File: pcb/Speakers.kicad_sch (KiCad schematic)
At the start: 34 parts, among them U4 ADA4891, U7 ADA4891

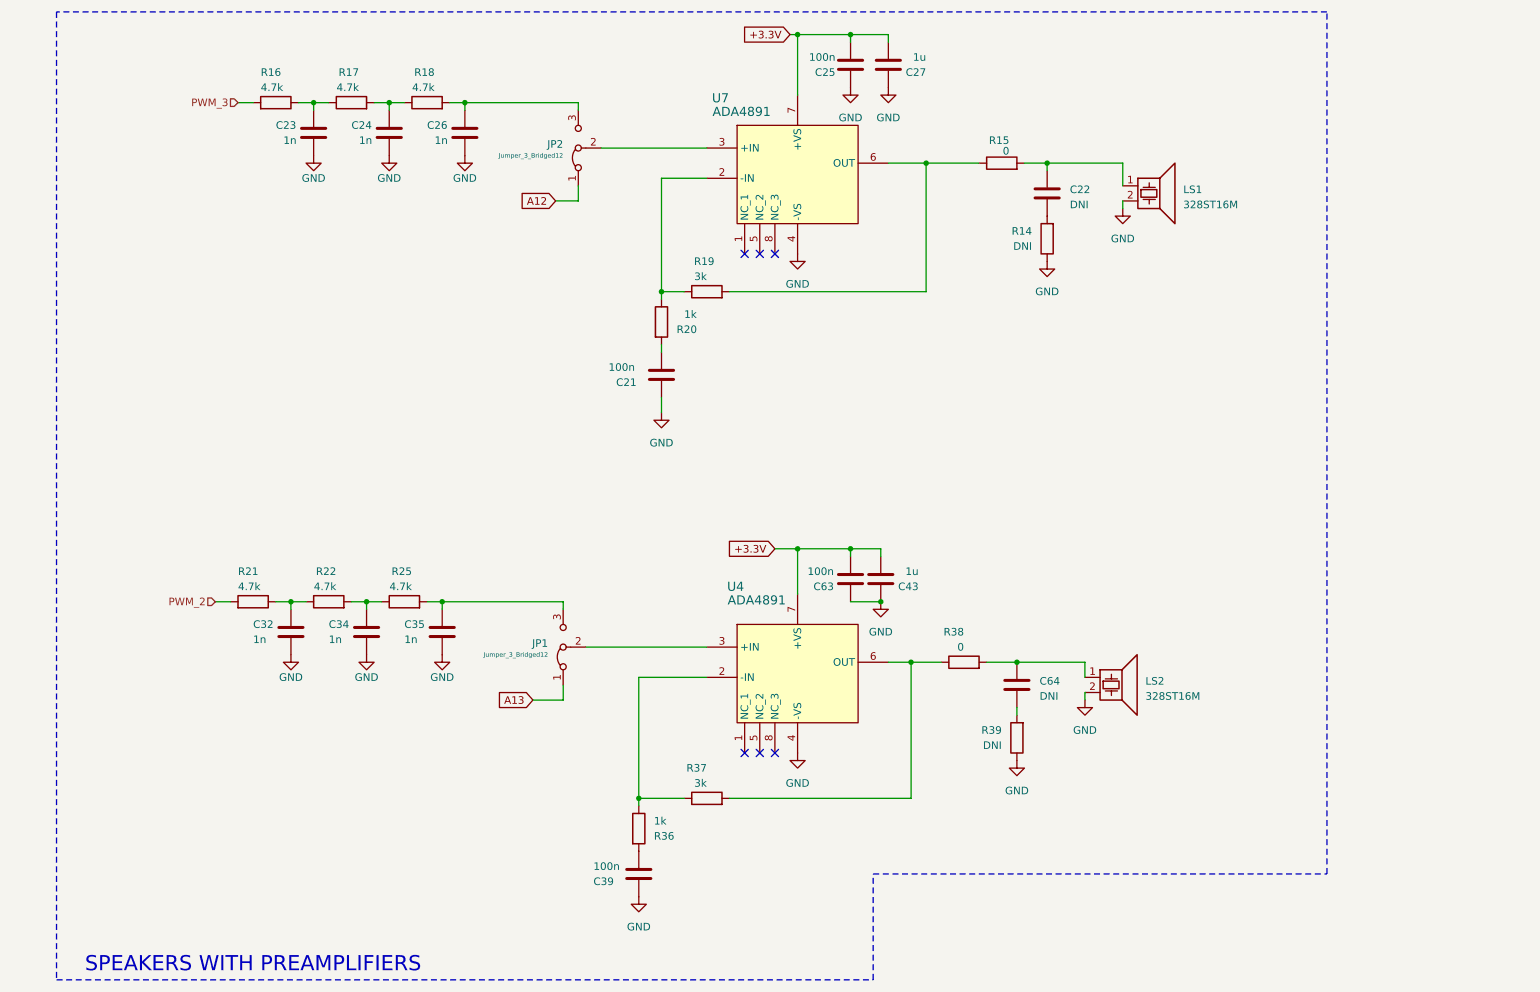
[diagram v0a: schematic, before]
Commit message: Progress in pcb routing
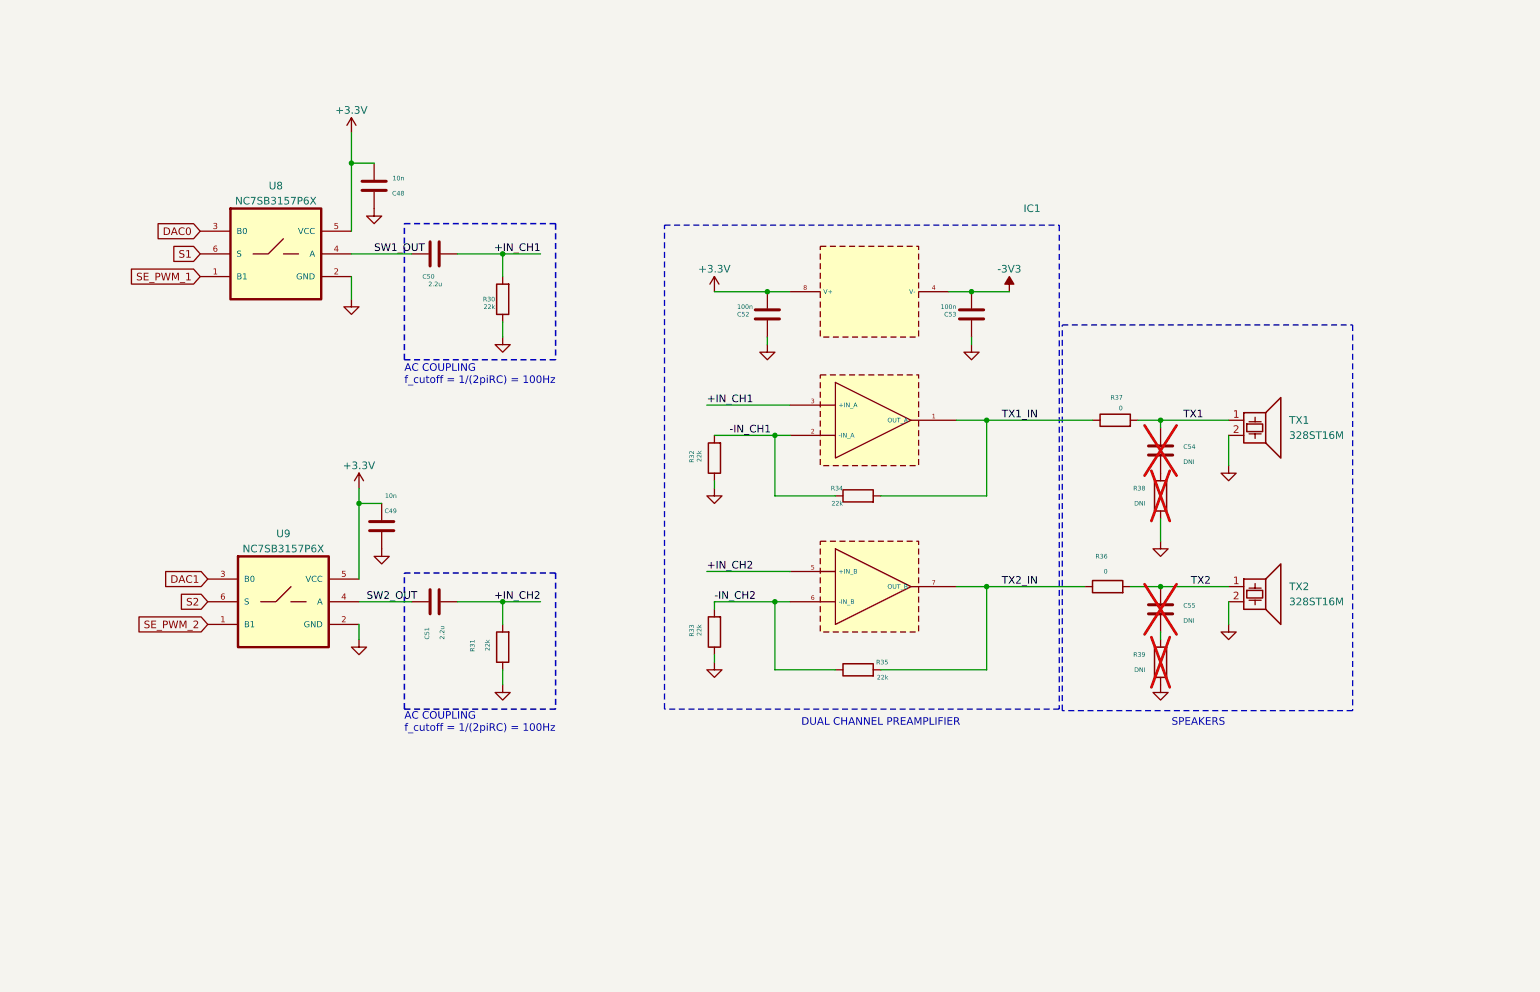
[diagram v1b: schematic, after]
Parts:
- removed C21, C25, C39, C63: 100n, Capacitor_SMD:C_0805_2012Metric, symbol Device:C
- removed C23, C24, C26, C32, C34, C35: 1n, Capacitor_SMD:C_0805_2012Metric, symbol Device:C
- removed C27, C43: 1u, Capacitor_SMD:C_0805_2012Metric, symbol Device:C
- removed JP1, JP2: Jumper_3_Bridged12, Connector_PinHeader_2.54mm:PinHeader_1x03_P2.54mm_Vertical, symbol Jumper:Jumper_3_Bridged12
- removed R16, R17, R18, R21, R22, R25: 4.7k, Resistor_SMD:R_0805_2012Metric, symbol Device:R
- removed R19, R37: 3k, Resistor_SMD:R_0805_2012Metric, symbol Device:R
- removed R20, R36: 1k, Resistor_SMD:R_0805_2012Metric, symbol Device:R
- removed U4, U7: ADA4891, SensEdu:ADA4891-1ARZ, symbol SensEdu:ADA4891-1ARZ
- added C48, C49: 10n, Capacitor_SMD:C_0805_2012Metric, symbol Device:C
- added C50, C51: 2.2u, Capacitor_SMD:C_0805_2012Metric, symbol Device:C
- added C52, C53: 100n, Capacitor_SMD:C_0805_2012Metric, symbol Device:C
- added IC1: ADA4511-2ARMZ, SensEdu:ADA4511, symbol SensEdu:ADA4511-2ARMZ
- added R30, R31, R32, R33, R34, R35: 22k, Resistor_SMD:R_0805_2012Metric, symbol Device:R
- added U8, U9: NC7SB3157P6X, SensEdu:SOT65P210X110-6N, symbol SensEdu:NC7SB3157P6X
- C54: renamed from C22; now not fitted
- C55: renamed from C64; now not fitted
- R38: renamed from R14; now not fitted
- R39: now not fitted
- renumbered R38 to R36, R15 to R37, LS1 to TX1, LS2 to TX2
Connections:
- net +3.3V: now also C48.2, C49.2, C52.1, IC1.8 (V+), U8.5 (VCC), U9.5 (VCC)
- net GND: now also C48.1, C49.1, C52.2, C53.1, R30.1, R31.1, R32.1, R33.1, U8.2 (GND), U9.2 (GND)
- net TX1_IN: now reaches R37.1
- net TX1_IN: now also IC1.1 (OUT_A), R34.2
- net TX2: now reaches C55.1, R36.2, TX2.1
- net TX1: now reaches C54.1, R37.2, TX1.1
- net TX2_IN: now reaches R36.1
- net TX2_IN: now also IC1.7 (OUT_B), R35.2
- new net +IN_CH1: C50.2, IC1.3 (+IN_A), R30.2
- new net +IN_CH2: C51.2, IC1.5 (+IN_B), R31.2
- new net -3V3: C53.2, IC1.4 (V-)
- new net -IN_CH1: IC1.2 (-IN_A), R32.2, R34.1
- new net -IN_CH2: IC1.6 (-IN_B), R33.2, R35.1
- new net DAC0: U8.3 (B0)
- new net DAC1: U9.3 (B0)
- new net S1: U8.6 (S)
- new net S2: U9.6 (S)
- new net SE_PWM_1: U8.1 (B1)
- new net SE_PWM_2: U9.1 (B1)
- new net SW1_OUT: C50.1, U8.4 (A)
- new net SW2_OUT: C51.1, U9.4 (A)
- no-connect marks 6 -> 0
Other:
- note added: "AC COUPLING f_cutoff = 1/(2piRC) = 100Hz"
- note added: "DUAL CHANNEL PREAMPLIFIER"
- note added: "SPEAKERS"
- note removed: "SPEAKERS WITH PREAMPLIFIERS"
- moved on the sheet: R36, R37, TX1, TX2

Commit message: pcb routing finished
very messy
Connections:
- net SE_PWM_2 is gone; now on net SE_PWM_1: U9.1 (B1)
- net SE_PWM_1: no longer U8.1 (B1)
- new net SE_PWM_3: U8.1 (B1)
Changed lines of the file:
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@@
 		)
 	)
-	(global_label "SE_PWM_2"
+	(global_label "SE_PWM_1"
 		(shape input)
 		(at 53.34 118.11 180)
@@
 		)
 	)
-	(global_label "SE_PWM_1"
+	(global_label "SE_PWM_3"
 		(shape input)
 		(at 52.07 59.69 180)

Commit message: in works
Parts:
- added C58: 1u, Capacitor_SMD:C_0805_2012Metric, symbol Device:C
- added C59: 100n, Capacitor_SMD:C_0805_2012Metric, symbol Device:C
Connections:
- net +3.3V: now also C58.1
- net -3V3: now also C59.1
- net GND: now also C58.2, C59.2
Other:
- note added: "1u another cap on both sides"
- title: SensEdu 0.7 -> SensEdu 0.9
- moved on the sheet: C52, C53

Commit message: fix: PCB final fixes
Added simulation for dc offset after ac coupling
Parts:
- added TP_TX1: TestPoint, TestPoint:TestPoint_THTPad_D2.0mm_Drill1.0mm, symbol Connector:TestPoint
- C50, C51: value 2.2u -> 100n
- C55: renamed from C59; value 100n -> 1u
- R30, R31: value 22k -> 1.2k
- renumbered C58 to C52, C52 to C53, C53 to C54, C54 to C56, C55 to C57
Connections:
- net +IN_CH1: now also TP_TX1.1
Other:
- note added: "AC COUPLING f_cutoff = 1/(2piRC) = 1kHz"
- note added: "should be a high quality film capacitor for best performance"
- note removed: "AC COUPLING f_cutoff = 1/(2piRC) = 100Hz"

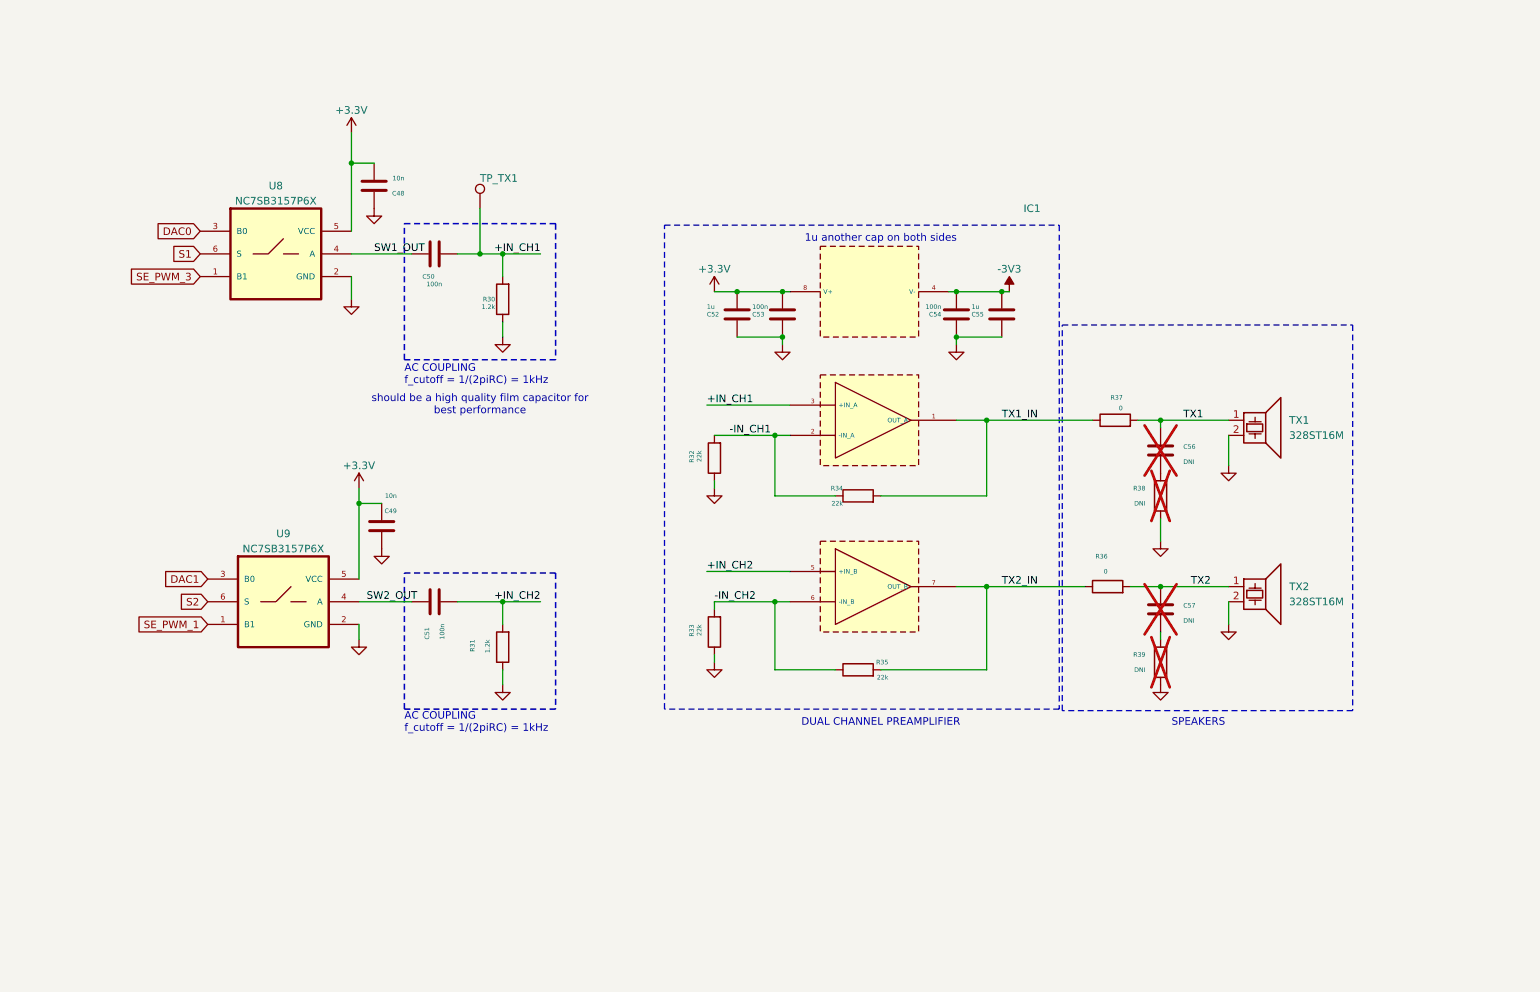
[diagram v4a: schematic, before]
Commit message: feat: Redraw PCB layout
- Change supply polarity and pin numbers of ADA4511
- Change cap of switches to 100n to reduce bom
- Change supply of sensors to unison 3.3V
- Rearrange mic and amps pins
- Add mountains
- Add Infineon logo
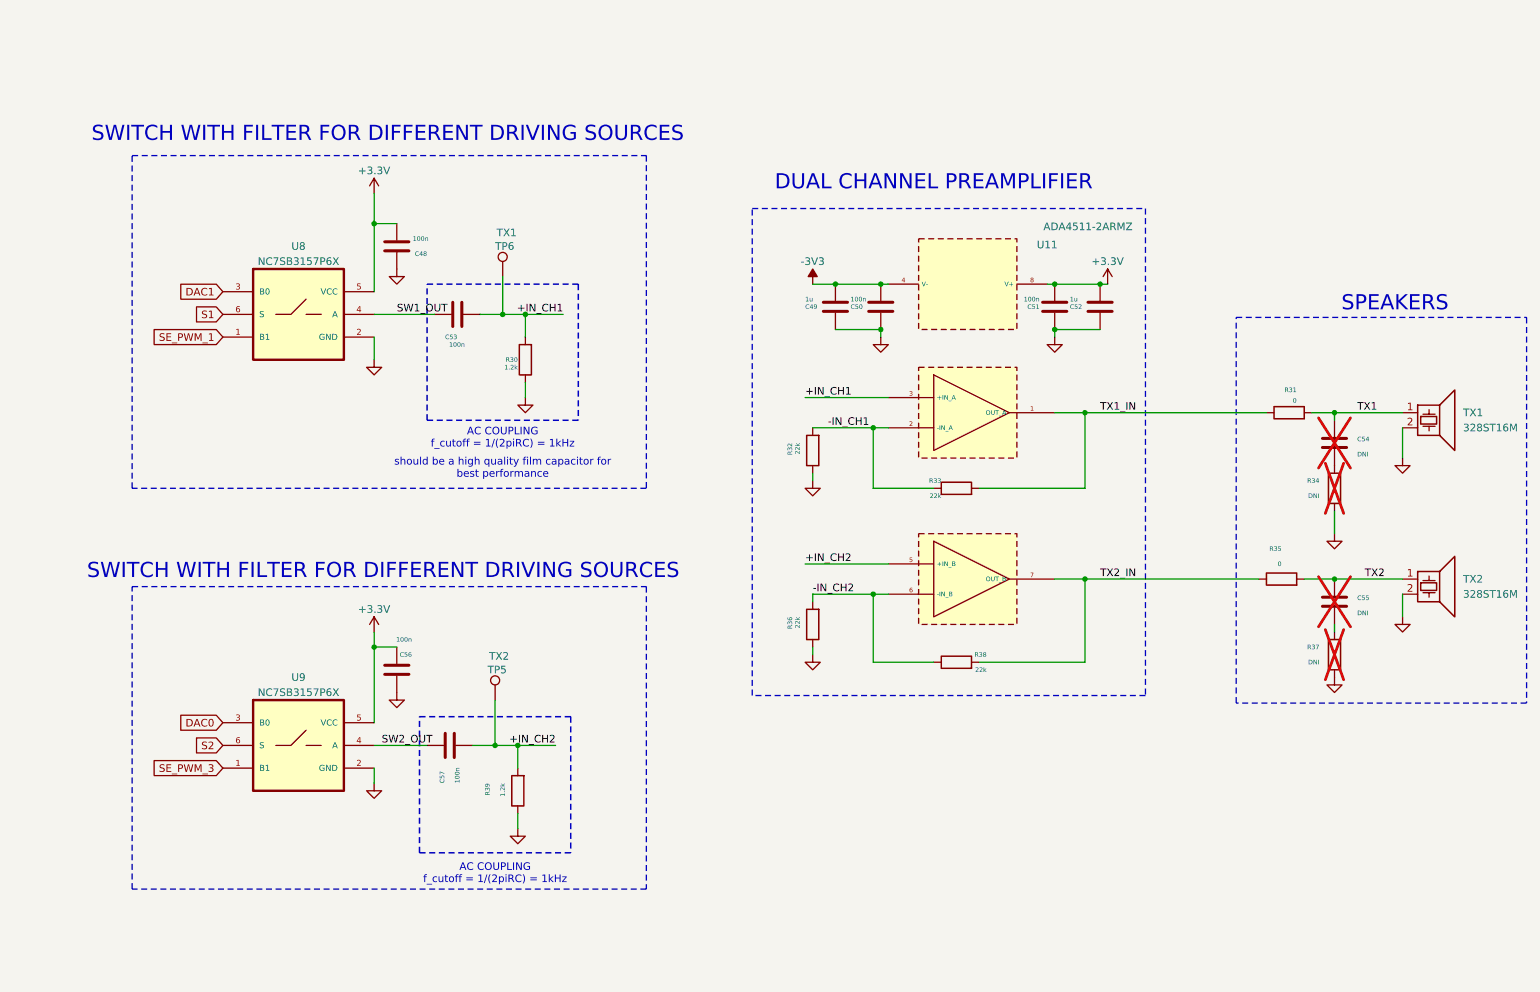
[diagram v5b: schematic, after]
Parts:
- added TP5: TX2, TestPoint:TestPoint_THTPad_D2.0mm_Drill1.0mm, symbol SensEdu:TestPoint
- C48: value 10n -> 100n; footprint Capacitor_SMD:C_0805_2012Metric -> Capacitor_SMD:C_0603_1608Metric; symbol Device:C -> SensEdu:C
- C49: renamed from C52; footprint Capacitor_SMD:C_0805_2012Metric -> Capacitor_SMD:C_0603_1608Metric; symbol Device:C -> SensEdu:C
- C50: renamed from C53; footprint Capacitor_SMD:C_0805_2012Metric -> Capacitor_SMD:C_0603_1608Metric; symbol Device:C -> SensEdu:C
- C51: renamed from C54; footprint Capacitor_SMD:C_0805_2012Metric -> Capacitor_SMD:C_0603_1608Metric; symbol Device:C -> SensEdu:C
- C52: renamed from C55; footprint Capacitor_SMD:C_0805_2012Metric -> Capacitor_SMD:C_0603_1608Metric; symbol Device:C -> SensEdu:C
- C53: renamed from C50; footprint Capacitor_SMD:C_0805_2012Metric -> Capacitor_SMD:C_0603_1608Metric; symbol Device:C -> SensEdu:C
- C54: renamed from C56; footprint Capacitor_SMD:C_0805_2012Metric -> Capacitor_SMD:C_0603_1608Metric; symbol Device:C -> SensEdu:C
- C55: renamed from C57; footprint Capacitor_SMD:C_0805_2012Metric -> Capacitor_SMD:C_0603_1608Metric; symbol Device:C -> SensEdu:C
- C56: renamed from C49; value 10n -> 100n; footprint Capacitor_SMD:C_0805_2012Metric -> Capacitor_SMD:C_0603_1608Metric; symbol Device:C -> SensEdu:C
- C57: renamed from C51; footprint Capacitor_SMD:C_0805_2012Metric -> Capacitor_SMD:C_0603_1608Metric; symbol Device:C -> SensEdu:C
- R30, R32: footprint Resistor_SMD:R_0805_2012Metric -> Resistor_SMD:R_0603_1608Metric; symbol Device:R -> SensEdu:R
- R31: renamed from R37; footprint Resistor_SMD:R_0805_2012Metric -> Resistor_SMD:R_0603_1608Metric; symbol Device:R -> SensEdu:R
- R33: renamed from R34; footprint Resistor_SMD:R_0805_2012Metric -> Resistor_SMD:R_0603_1608Metric; symbol Device:R -> SensEdu:R
- R34: renamed from R38; footprint Resistor_SMD:R_0805_2012Metric -> Resistor_SMD:R_0603_1608Metric; symbol Device:R -> SensEdu:R
- R35: renamed from R36; footprint Resistor_SMD:R_0805_2012Metric -> Resistor_SMD:R_0603_1608Metric; symbol Device:R -> SensEdu:R
- R36: renamed from R33; footprint Resistor_SMD:R_0805_2012Metric -> Resistor_SMD:R_0603_1608Metric; symbol Device:R -> SensEdu:R
- R37: renamed from R39; footprint Resistor_SMD:R_0805_2012Metric -> Resistor_SMD:R_0603_1608Metric; symbol Device:R -> SensEdu:R
- R38: renamed from R35; footprint Resistor_SMD:R_0805_2012Metric -> Resistor_SMD:R_0603_1608Metric; symbol Device:R -> SensEdu:R
- R39: renamed from R31; footprint Resistor_SMD:R_0805_2012Metric -> Resistor_SMD:R_0603_1608Metric; symbol Device:R -> SensEdu:R
- TP6: renamed from TP_TX1; value TestPoint -> TX1; symbol Connector:TestPoint -> SensEdu:TestPoint
- TX1, TX2: symbol Device:Speaker_Ultrasound -> SensEdu:Speaker_Ultrasound
- U11: renamed from IC1; footprint SensEdu:ADA4511 -> SamacSys_Parts:SOP65P490X110-8N
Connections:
- net +3.3V: now also C51.2, C52.1; no longer C49.1, C50.1
- net +IN_CH2: now also TP5.1
- net -3V3: now also C49.1, C50.1; no longer C51.2, C52.1
- net DAC0: now also U9.3 (B0); no longer U8.3 (B0)
- net DAC1: now also U8.3 (B0); no longer U9.3 (B0)
- net SE_PWM_1: now also U8.1 (B1); no longer U9.1 (B1)
- net SE_PWM_3: now also U9.1 (B1); no longer U8.1 (B1)
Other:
- note added: "SWITCH WITH FILTER FOR DIFFERENT DRIVING SOURCES"
- note removed: "1u another cap on both sides"
- moved on the sheet: C48, C49, C50, C51, C52, C53, C54, C55, C56, C57, R30, R31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

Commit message: refactor: Update PDF and information
- Add BOM
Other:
- title: SensEdu 0.9 -> SensEdu
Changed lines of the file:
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@@
 	(paper "A4")
 	(title_block
-		(title "SensEdu 0.9")
-		(date "2025-12-05")
+		(title "SensEdu")
+		(date "2026-02-26")
 		(rev "0.9")
 		(company "Infineon Technologies")
